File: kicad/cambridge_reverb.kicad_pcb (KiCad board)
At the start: 2 copper layers, 190 x 115 mm, 143 parts, among them IC1 TL072CP, IC2 TL072CP, Q1 MMBF5457, Q2 MMBF5457, T1 reuse / AnTek AS-0524, U1 LM317T

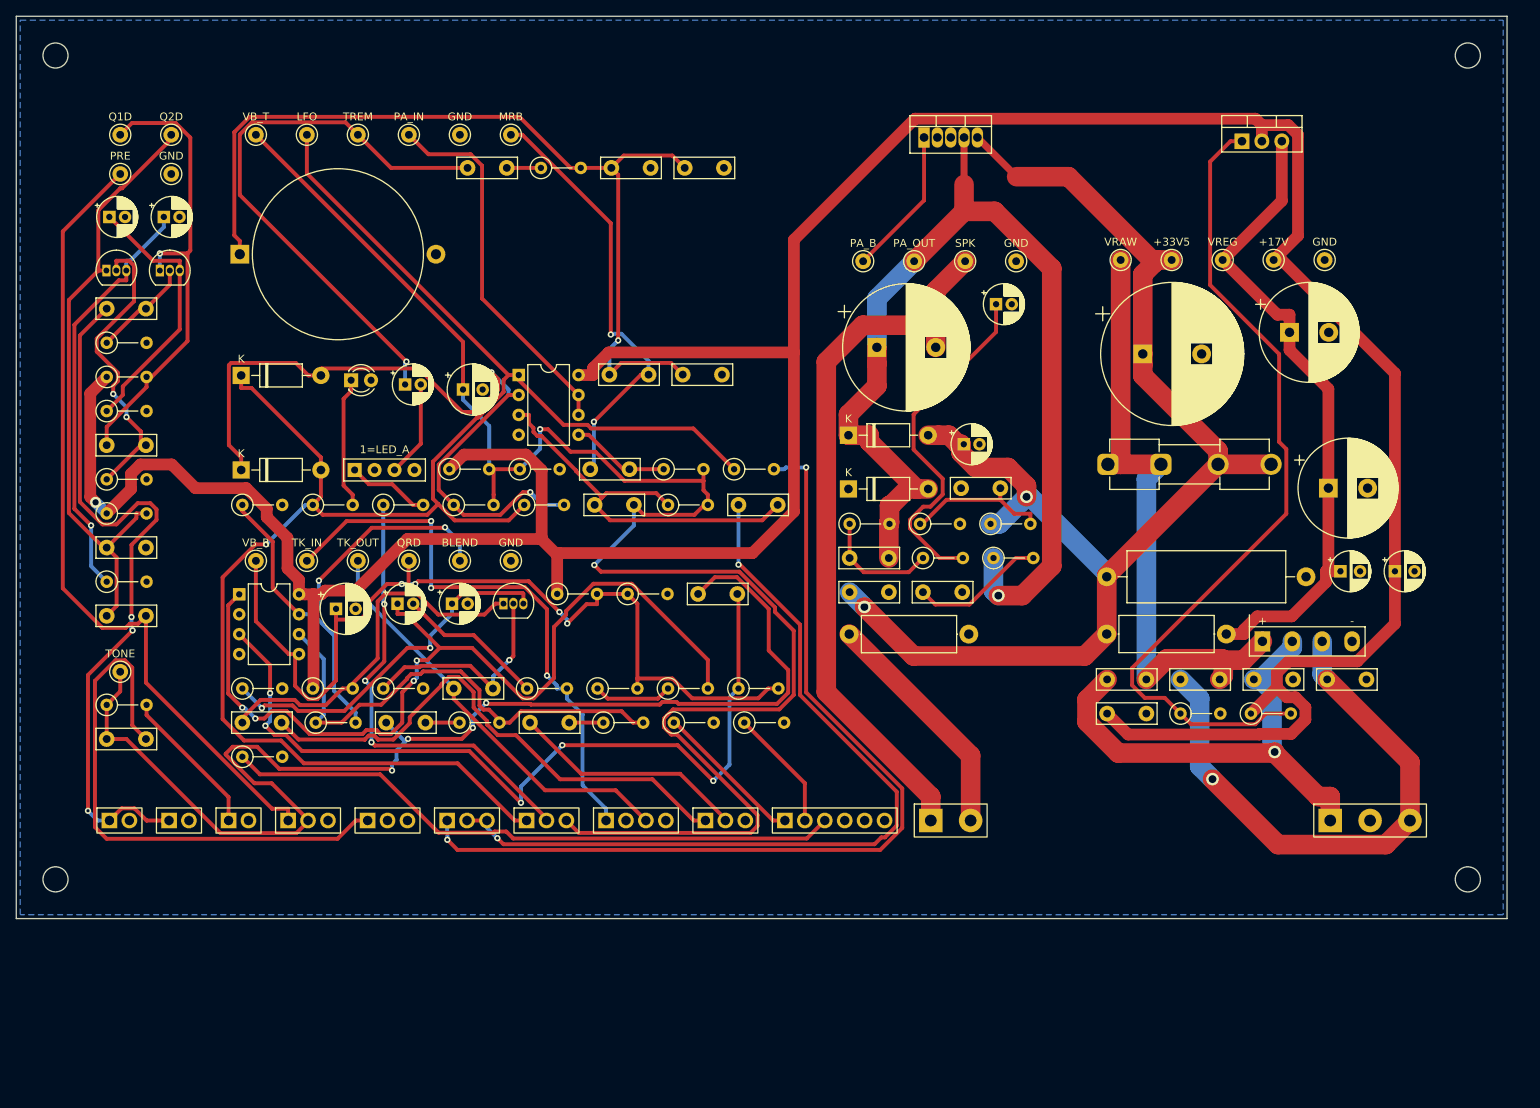
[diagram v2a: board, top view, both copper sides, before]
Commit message: Mixed SMD/THT variant (kicad/smd, 155x90), JFET pin-number fix, THT fully routed
Build profiles: gen_kicad.py / gen_pcb.py / gen_bom.py take --profile tht|smd.
One schematic source; the smd profile remaps footprints and writes a self-
contained KiCad project to kicad/smd/ (cambridge_reverb_smd.*, lib tables one
level up), sized 155 x 90 mm for the Part 7 safe-bet chassis.

SMD (70 parts): 0805 R (1206 for R_reg2), 1206 C <= 100 nF, 1210 for 120 nF /
1 uF / C_zobel, SMA + SOD-123 diodes, SOT-23 JFETs fitted directly.
Deliberately THT: power parts, all electrolytics (standing cans use less board
than SMD cans), DIP-8 sockets for the TL072s, the three bench-trimmed JFET
source resistors, LED, connectors, test points. Parts area 4560 mm^2 -> 48 % of
the 155x90 usable area (THT 60 %).

SMD board specifics: 6 mm margin, 0.6 mm gap, 3 mm channels, pad row clear of
the corner holes; GND pour on both layers (top pour solid to SMD ground pads
only, router sees just the bottom plane so every SMD ground pad gets a via);
HighCurrent/Power classes 2.0/1.0 mm for this board (errata #11 addendum).
Routed: 165/167 connections, 1 DRC error (starved thermal), 109 vias; the two
open items are listed in PCB-NOTES as GUI touches. Eight router settings and
three pour strategies compared; the committed one is the best of them.

Errata #18 (HIGH): the JFET symbol had 2 = Gate / 3 = Source; onsemi's 2N5457
(TO-92) and MMBF5457 (SOT-23) both number the leads 1 D / 2 S / 3 G, so the THT
board would have swapped gate and source on Q1, Q2, Q_rec. Symbol renumbered,
both boards regenerated. THT board re-routed (also fixed the column balance):
166/166 connections, 0 DRC violations, 66 vias -- fully routed.

Also: bom/bom-smd*.csv (spec notes, no invented P/Ns), production/smd/
bom-jlcpcb.csv + position file + README for JLCPCB assembly of the SMD side;
route_board.py --drop-planes and default via cost 60; docs (PCB-NOTES,
PCB-AUDIT, README, CHANGELOG, errata, availability audit, Part 10, kicad and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
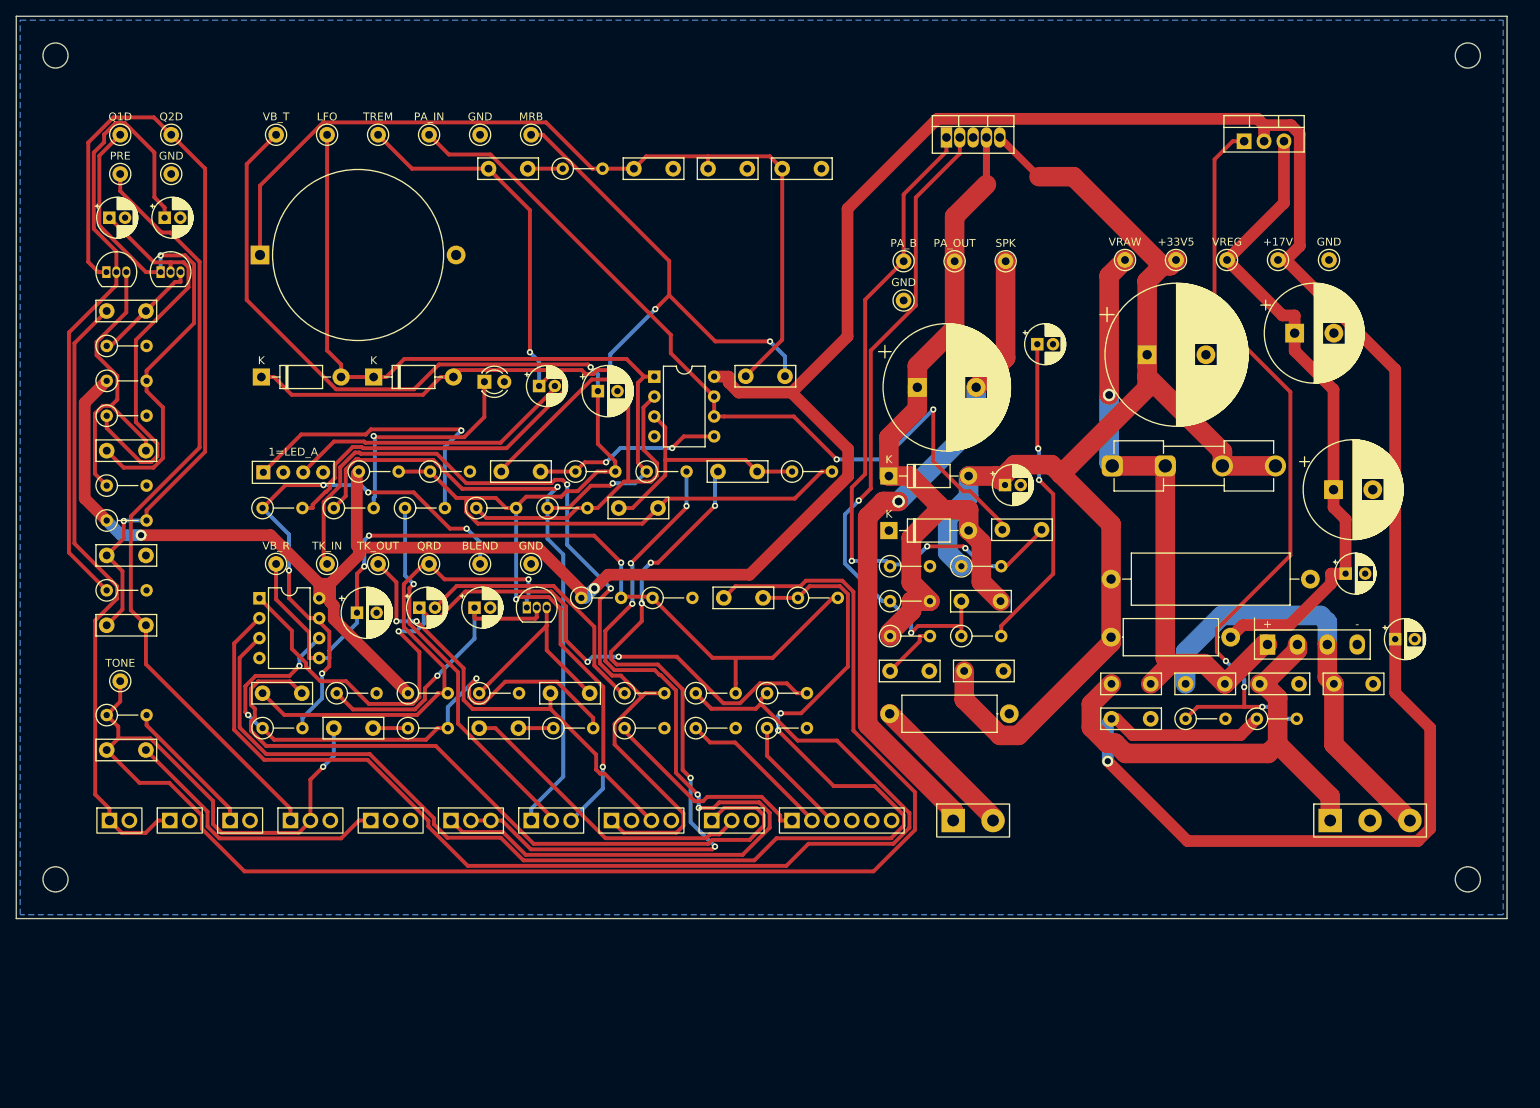
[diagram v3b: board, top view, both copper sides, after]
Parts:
- moved R_fs_mrb 67.0 mm to (95.7, 90.7)
- moved C_mrb_750 29.2 mm to (97.6, 19.4)
- moved C_byp1 17.7 mm to (120.8, 83.4)
- moved C_mrb_out 17.4 mm to (93.0, 45.9)
- moved IC2 17.3 mm to (81.3, 45.9)
- moved C_vbt 17.2 mm to (74.1, 47.8)
- moved C_dc_blk 17.1 mm to (66.6, 47.1)
- moved LED_rate 17.0 mm to (59.7, 46.6)
- moved D_lfo1 16.9 mm to (45.5, 46.0)
- moved R_zobel 16.5 mm to (111.4, 79.0)
- moved R_lfo1 16.4 mm to (98.9, 58.0)
- moved C_fb_hf 15.3 mm to (120.4, 74.5)
- moved TP_GND_PA 15.2 mm to (113.1, 36.2)
- moved R_drvbias 13.8 mm to (99.6, 74.1)
- moved R_drv1 12.6 mm to (95.7, 86.3)
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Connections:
- Q1 pad 2: Q1G -> Q1S
- Q1 pad 3: Q1S -> Q1G
- Q2 pad 2: Q2G -> Q2S
- Q2 pad 3: Q2S -> Q2G
- Q_rec pad 2: QRG -> QRS
- Q_rec pad 3: QRS -> QRG
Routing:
- net R_INV: track 10.1 -> 148.9 mm
- net PA_INV: track 15.2 -> 84.5 mm, vias 0 -> 2
- net FS_MRB: track 79.6 -> 15.2 mm
- net PA_IN: track 47.8 -> 106.4 mm, vias 0 -> 2
- net TONE_OUT: track 161.3 -> 219.9 mm, vias 4 -> 1
- net DRVP: track 106.0 -> 162.6 mm, vias 5 -> 2
- net PA_BIAS: track 37.8 -> 87.6 mm, vias 0 -> 3
- net LFO_OUT: track 225.5 -> 181.2 mm, vias 1 -> 2
- net TANK_IN: track 73.2 -> 112.7 mm, vias 3 -> 2
- net PA_OUT: track 134.4 -> 96.0 mm, vias 1 -> 0
- net TCW: track 71.0 -> 35.4 mm
- net Q2S: track 53.8 -> 81.8 mm, vias 1 -> 0
- net VLED: track 10.6 -> 38.3 mm, vias 0 -> 1
- net REVWCW: track 68.2 -> 94.6 mm
- net MRB_OUT: track 55.3 -> 81.7 mm, vias 2 -> 3
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
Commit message: SPICE parameter sweeps with committed results; tremolo LFO fix (errata #19); re-route
spice/: six ngspice sweeps next to the fixed-point checks, and run_all.sh now
saves every result table to spice/results/ (committed evidence):
- sweep_preamp_bias: Vd vs R_s for LO/TYP/HI JFET corners (datasheet Idss 1/3/5
  mA). The recovered 2.2k suits a HIGH-Idss part (8.8 V); a typical part wants
  ~1.0k (8.5 V); a 1 mA part cannot reach 8-9 V at any R_s -> errata #15 quantified
- sweep_tonestack: response over the whole pot travel (1 kHz -1.6..-3.3 dB while
  10 kHz falls 14 dB)
- sweep_lfo_speed_recovered: the recovered single-arm Wien LFO oscillates only for
  pot <= ~27k (5 % of travel) at 45-80 Hz, and not at all elsewhere
- sweep_lfo_speed: the fixed network, 10.6 Hz .. 0.60 Hz at constant 0.96 Vpp
- sweep_classa_bias: standing current / heat / THD vs bias (1.4 % -> 0.002 %,
  0.11 -> 0.85 A)
- sweep_pa_headroom: clean power vs rail, mains -10 %..+10 % = 8.9 / 11.7 / 14.8 W

Errata #19 (HIGH): the tremolo LFO did not work as recovered (Wien start condition
gain > 2 + R1/R2 fails with the speed pot in one arm). Built design: dual-gang
250k lin speed pot (one gang per arm, same panel hole), 15k floors, 1 uF timing
caps; POT_SPD_A/B in schematic + BOM = one part. tran_tremolo_lfo.cir aligned
(10.59 Hz at the fast end). Docs: errata, Part 1 s5, Part 2 note, Part 6b, BOM
cross-check, spice README (sweep tables), PCB-NOTES test-point row, README.

Both boards regenerated and re-routed (six settings each; Freerouting is
deterministic per input but placement-sensitive): THT 167/168, 3 starved-thermal
errors (was 166/166 clean); SMD 162/169, DRC clean (was 165/167 + 1 error).
Reports in kicad/reports/, open links listed in PCB-NOTES.

Co-Authored-By: Claude Fable 5.1 <noreply@anthropic.com>
Claude-Session: https://claude.ai/code/session_01Vk8HkvCugxFpQsBPVnNT2H
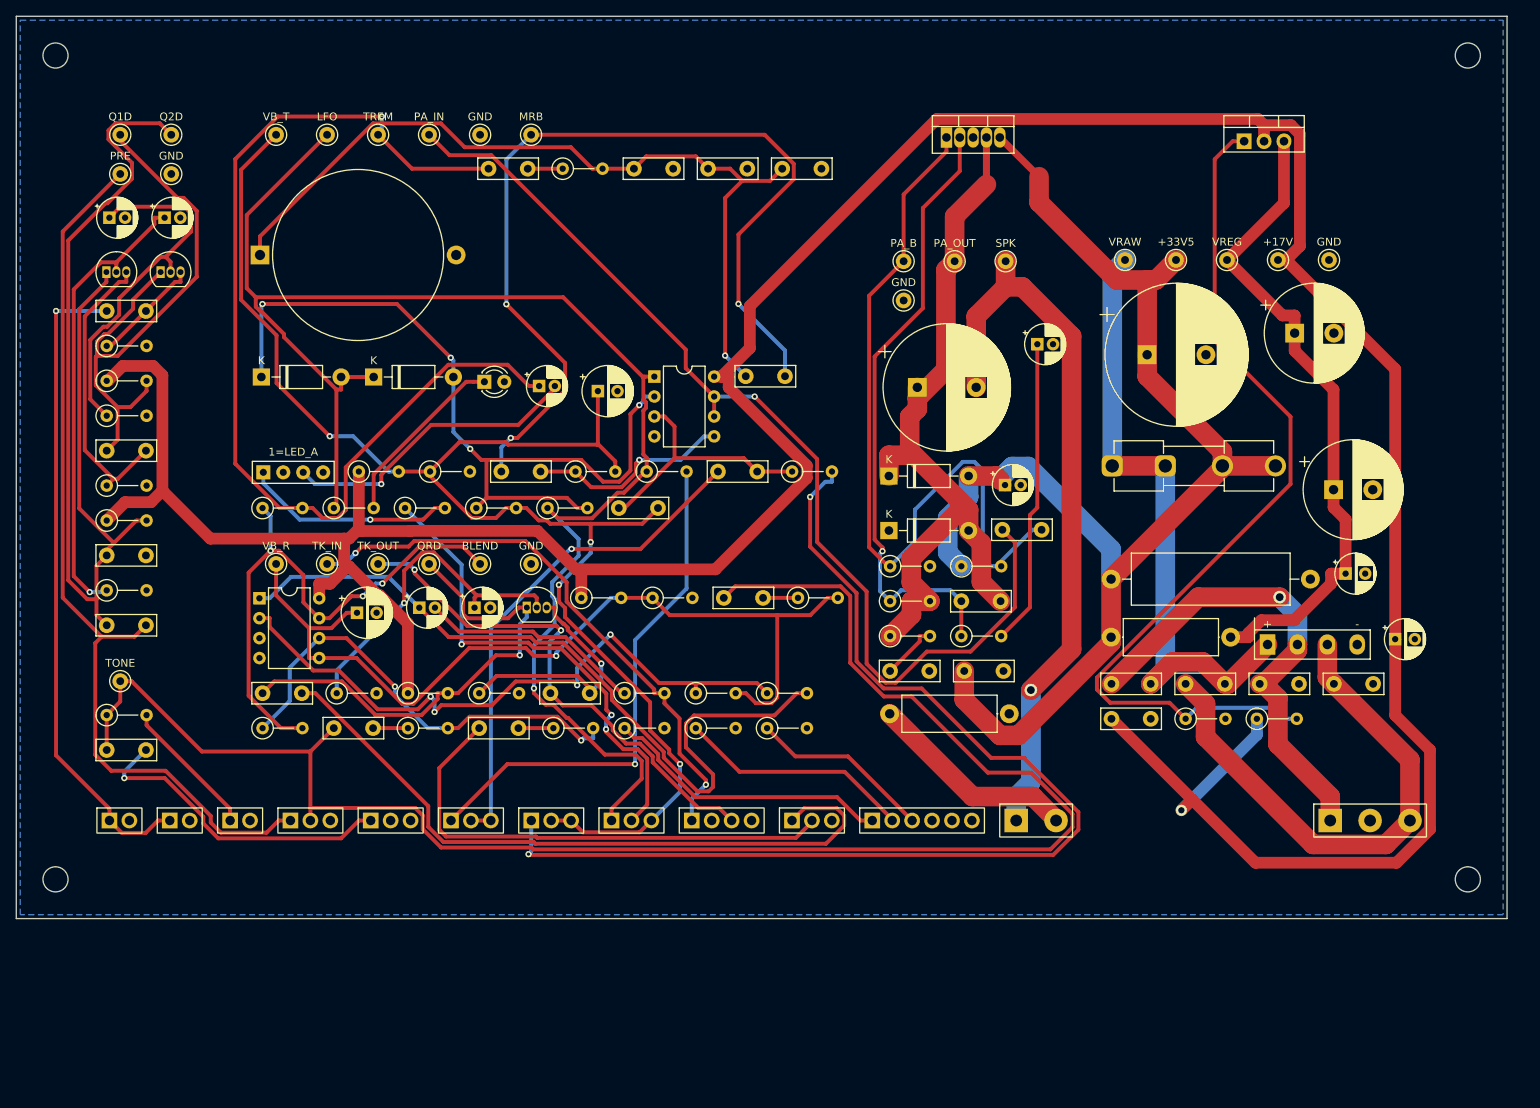
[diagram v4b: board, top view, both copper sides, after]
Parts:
- removed POT_SPD: 500k lin, WirePad_1x03_P2.54mm_D1.2mm
- removed R_lfo1: 33k, R_Axial_DIN0207_L6.3mm_D2.5mm_P5.08mm_Vertical
- added POT_SPD_A: 250k lin dual, WirePad_1x03_P2.54mm_D1.2mm, F.Cu at (55.4, 102.5)
- added POT_SPD_B: 250k lin dual, WirePad_1x03_P2.54mm_D1.2mm, F.Cu at (65.6, 102.5)
- added R_lfo_sh: 15k, R_Axial_DIN0207_L6.3mm_D2.5mm_P5.08mm_Vertical, F.Cu at (98.9, 58.0)
- C_lfo1, C_lfo2: value 100nF -> 1uF
- R_lfo_ser: value 10k -> 15k
- moved FS1 10.2 mm to (109.1, 102.5)
- moved REV1 10.2 mm to (86.1, 102.5)
- moved POT_DPT 10.2 mm to (75.9, 102.5)
- moved POT_REV 10.2 mm to (98.9, 102.5)
- moved LS1 8.03 mm to (127.4, 102.5)
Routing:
- net DRVP: track 162.6 -> 4.45 mm, vias 2 -> 0
- net SPD_B: track 0.00 -> 142.7 mm, vias 0 -> 2
- net R_INV: track 148.9 -> 82.7 mm, vias 0 -> 4
- net SPD_A: track 111.0 -> 66.4 mm, vias 5 -> 1
- net TANK_IN: track 112.7 -> 73.1 mm
- net TREM_OUT: track 92.8 -> 132.1 mm
- net MRB_OUT: track 81.7 -> 118.6 mm
- net WN1: track 95.4 -> 64.3 mm, vias 5 -> 1
- net VBIAS_T: track 219.6 -> 189.3 mm, vias 3 -> 4
- net PA_IN: track 106.4 -> 133.6 mm, vias 2 -> 1
- net Q2D: track 103.7 -> 130.8 mm, vias 1 -> 0
- net WET: track 39.0 -> 64.0 mm
- net Q2S: track 81.8 -> 58.8 mm, vias 0 -> 1
- net LFO_OUT: track 181.2 -> 200.6 mm, vias 2 -> 1
- net SUMJ: track 74.8 -> 58.0 mm, vias 3 -> 2
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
